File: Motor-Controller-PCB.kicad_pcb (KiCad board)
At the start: 2 copper layers, 68.6 x 53.3 mm, 33 parts, among them Q1 IFX007T, Q2 TJ200F04M3L, Q3 TJ200F04M3L, U1 DS18B20-PAR

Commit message: Update Motor-Controller-PCB.kicad_pcb
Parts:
- removed the C11 at (149.4, 90.5)
- removed the C11 at (149.4, 88.3)
- removed the C14 at (160.5, 86.6)
- removed the C14 at (160.5, 84.3)
- removed the C5 at (120.7, 94.8)
- removed the C5 at (122.9, 94.7)
- removed the C6 at (149.9, 83.8)
- removed the C6 at (149.9, 86.2)
- removed the REF** at (177.5, 109.6)
- removed the REF** at (177.8, 72.8)
- removed the REF** at (119.6, 82.7)
- removed the REF** at (125.4, 103.4)
- added C11: 100nF, Capacitor_SMD:C_0805_2012Metric_Pad1.18x1.45mm_HandSolder, B.Cu at (139.4, 105.9)
- added C14: 100nF, Capacitor_SMD:C_0805_2012Metric_Pad1.18x1.45mm_HandSolder, B.Cu at (153.8, 77.8)
- added C5: 220nF, Capacitor_SMD:C_0805_2012Metric_Pad1.18x1.45mm_HandSolder, B.Cu at (128.6, 96.2)
- added C6: 220nF, Capacitor_SMD:C_0805_2012Metric_Pad1.18x1.45mm_HandSolder, B.Cu at (151.2, 77.8)
- added REF**: GiantMetalCube, Motor-Controller-PCB:GiantMetalCube, B.Cu at (129.2, 82.0)
- added REF**: GiantMetalCube, Motor-Controller-PCB:GiantMetalCube, B.Cu at (182.8, 116.7)
- added REF**: GiantMetalCube, Motor-Controller-PCB:GiantMetalCube, B.Cu at (128.3, 109.2)
- added REF**: GiantMetalCube, Motor-Controller-PCB:GiantMetalCube, B.Cu at (174.1, 90.2)
- A1: moved to F.Cu
- moved A1 53.4 mm to (184.1, 70.1)
- moved R5 43.6 mm to (151.4, 118.8)
- moved R14 43.0 mm to (148.4, 74.8), turned to 0 degrees
- moved R1 42.8 mm to (135.0, 117.4), turned to 270 degrees
- moved C1 42.3 mm to (130.0, 75.2), turned to 180 degrees
- moved R4 39.6 mm to (157.3, 78.1), turned to 90 degrees
- moved R13 37.9 mm to (147.4, 78.0), turned to 90 degrees
- moved Q2 22.2 mm to (157.1, 86.0)
- moved D3 21.6 mm to (156.0, 111.8), turned to 270 degrees
- moved Q3 20.4 mm to (159.2, 111.0), turned to 90 degrees
- moved Q1 19.9 mm to (128.7, 104.5)
- moved R2 19.4 mm to (130.8, 78.5), turned to 90 degrees
- moved C7 11.6 mm to (178.0, 98.6), turned to 90 degrees
- moved D1 10.6 mm to (156.0, 105.5), turned to 90 degrees
- moved D2 10.3 mm to (159.3, 103.4), turned to 0 degrees
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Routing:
- net GND: track 69.8 -> 34.1 mm
- net Net-(A1-Pad10): track 36.9 -> 4.42 mm
- net Net-(Q1-Pad6): track 7.34 -> 39.1 mm
- net Net-(C2-Pad2): track 42.7 -> 70.8 mm
- net Net-(Q1-Pad3): track 16.5 -> 38.6 mm
- net Net-(D3-Pad2): track 9.40 -> 22.6 mm
- net Net-(A1-Pad17): track 41.4 -> 33.5 mm
- net Net-(C14-Pad1): track 29.6 -> 21.7 mm
- net Net-(A1-Pad12): track 36.4 -> 29.3 mm
- net OUT_1: track 15.1 -> 8.21 mm
- net VBAT: track 4.78 -> 0.00 mm
- net Net-(A1-Pad15): track 22.2 -> 26.9 mm
- net Net-(A1-Pad18): track 3.77 -> 8.19 mm
- net Net-(C11-Pad1): track 6.78 -> 4.04 mm
- net Net-(A1-Pad5): track 50.8 -> 48.0 mm
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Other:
- outline, holes or cut-outs redrawn

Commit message: pins and silkscreen
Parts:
- added G***: LOGO, Motor-Controller-PCB:AELogo, F.Cu at (140.2, 114.9)
- added LOGO: , Motor-Controller-PCB:LOGO (7), F.Cu at (115.7, 70.1)
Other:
- board text added: "2021 applied engineering"
- board text added: "DC Motor Control Board Rev. 2021-04-28"

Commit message: halftone
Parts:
- removed the G*** at (140.2, 114.9)
- added G***: LOGO, Motor-Controller-PCB:LogoAE, F.Cu at (140.2, 114.9)

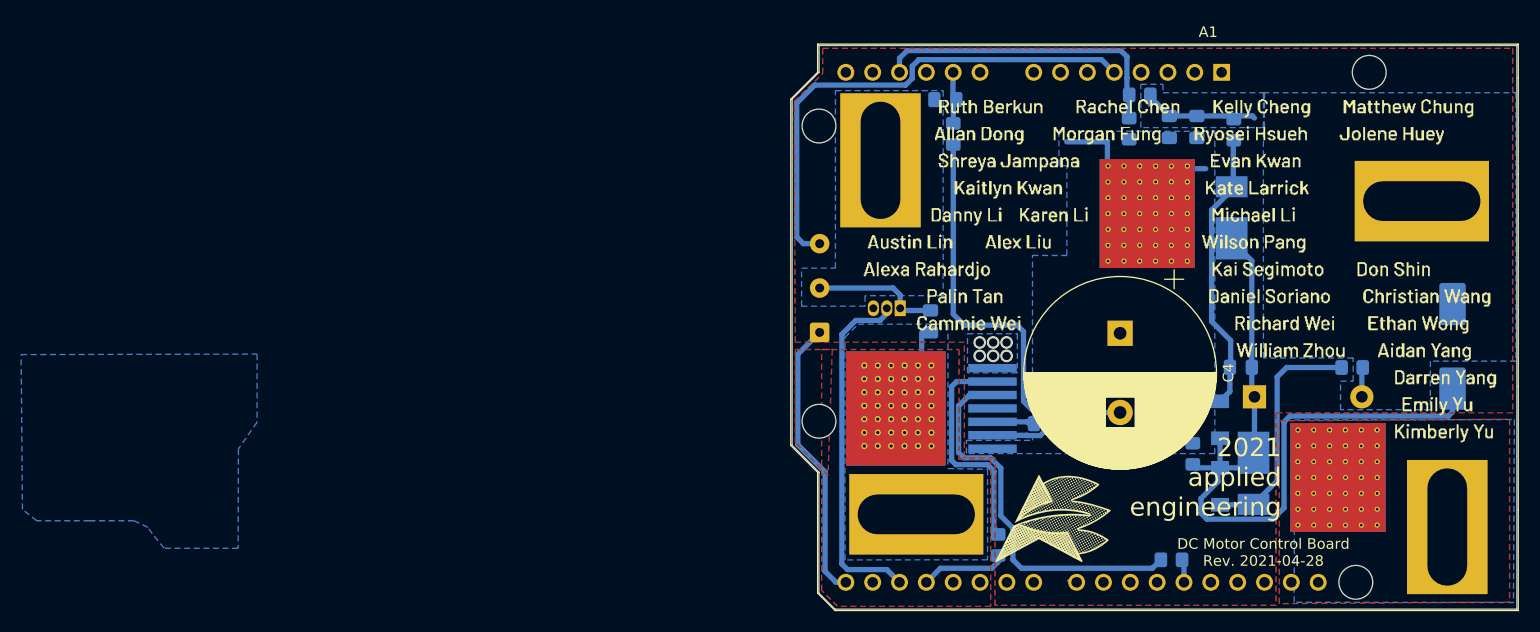
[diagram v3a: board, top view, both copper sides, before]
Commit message: silkscreen fixes
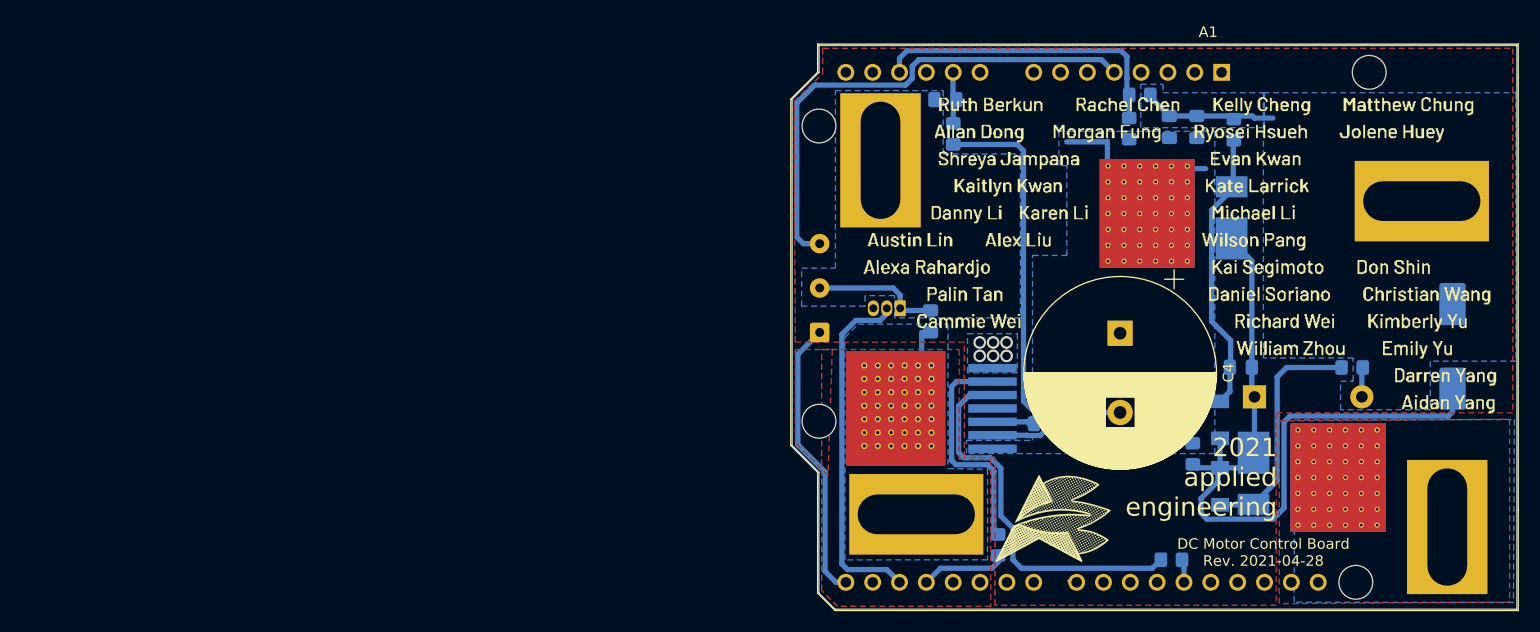
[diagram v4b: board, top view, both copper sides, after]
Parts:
- removed the LOGO at (115.7, 70.1)
- added LOGO: , Motor-Controller-PCB:LOGO (11), F.Cu at (115.7, 69.9)
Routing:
- net GND: track 34.1 -> 34.9 mm
- net Net-(Q1-Pad6): track 39.1 -> 39.7 mm
